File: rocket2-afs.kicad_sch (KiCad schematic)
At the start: 68 parts, among them J1 ARMING_PLUG, J2 POWER, J3 E-MATCH_DROGUE, J4 SWD, J5 E-MATCH_RECOVERY, Q1 Q_NMOS_GSD, Q2 Q_NMOS_GSD, Q3 Q_NMOS_GSD, Q4 Q_NMOS_GSD, Q5 Q_NMOS_GSD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

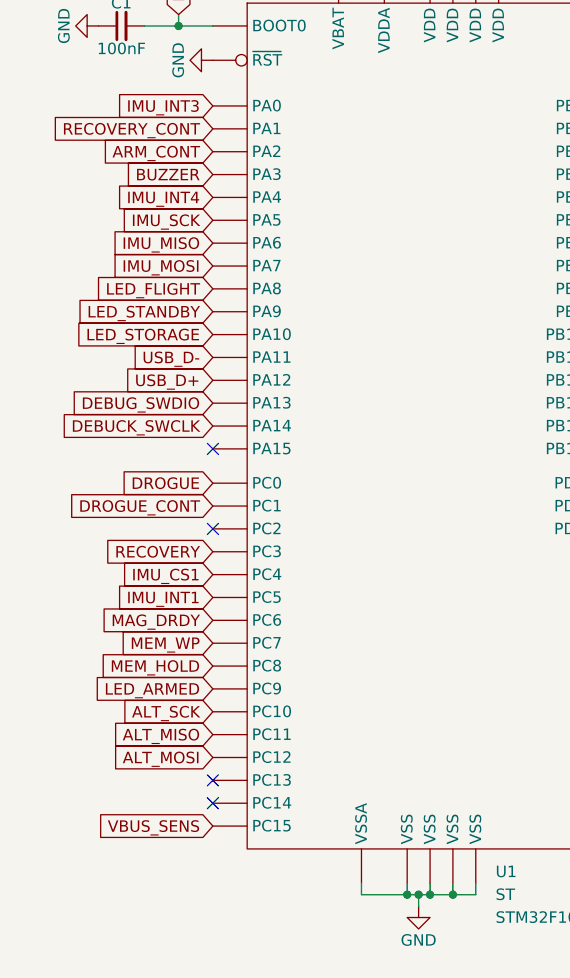
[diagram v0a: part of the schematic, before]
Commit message: Moved All Thick Components to "Front" Layer. Added Silkscreens
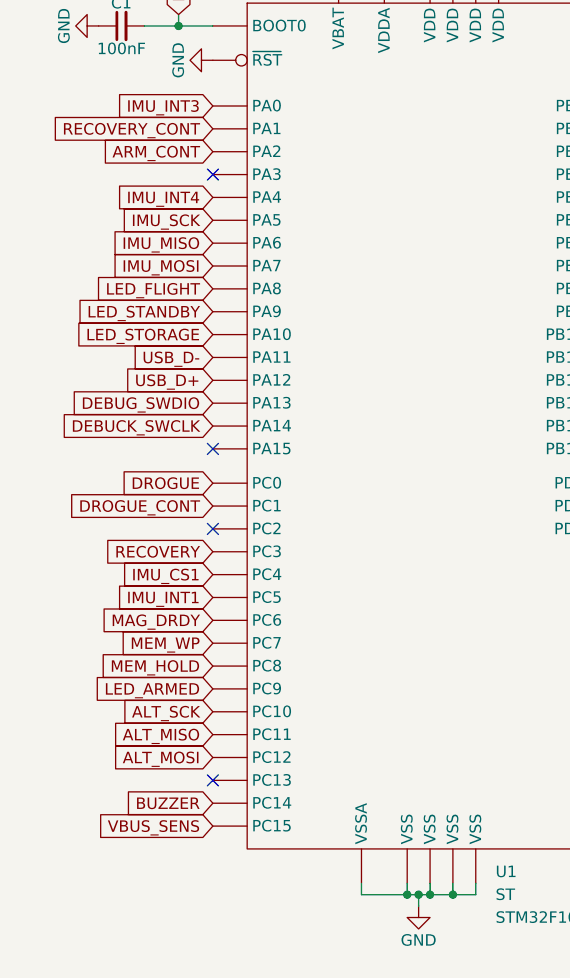
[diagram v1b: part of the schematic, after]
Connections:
- net BUZZER: now also U1.3 (PC14); no longer U1.17 (PA3)
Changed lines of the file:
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@@
   (no_connect (at 173.99 118.11))
   (no_connect (at 78.74 101.6))
+  (no_connect (at 33.02 64.77))
   (no_connect (at 78.74 67.31))
   (no_connect (at 124.46 151.13))
@@
   (no_connect (at 199.39 109.22))
   (no_connect (at 33.02 132.08))
-  (no_connect (at 33.02 134.62))
   (no_connect (at 124.46 153.67))
   (no_connect (at 199.39 111.76))
@@
     )
   )
-  (global_label "BUZZER" (shape input) (at 33.02 64.77 180) (fields_autoplaced)
+  (global_label "BUZZER" (shape input) (at 33.02 134.62 180) (fields_autoplaced)
     (effects (font (size 1.27 1.27)) (justify right))
-    (property "Intersheetrefs" "${INTERSHEET_REFS}" (at 22.5963 64.77 0)
+    (property "Intersheetrefs" "${INTERSHEET_REFS}" (at 22.5963 134.62 0)
       (effects (font (size 1.27 1.27)) (justify right) hide)
     )

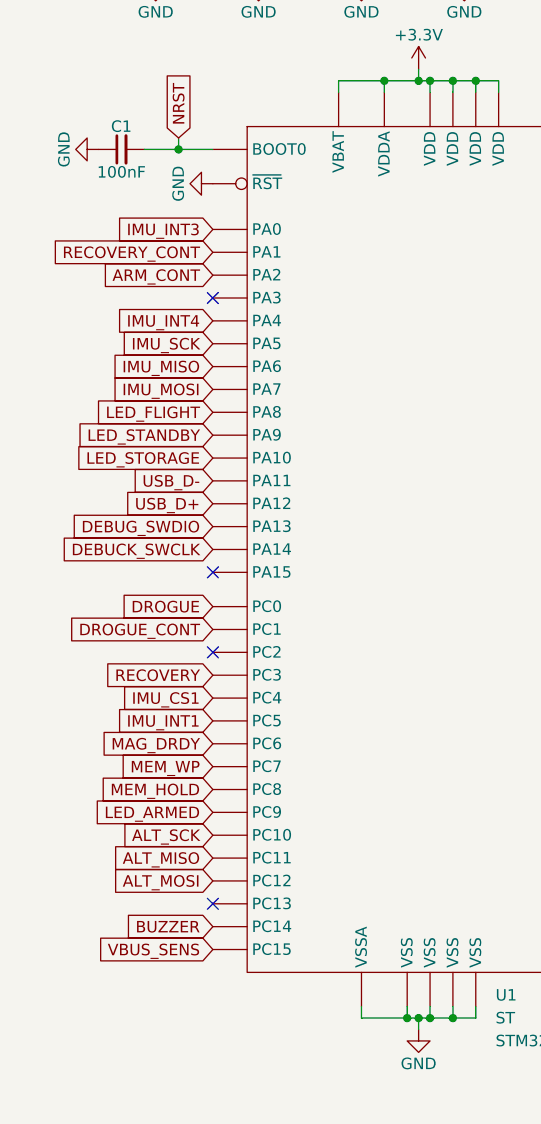
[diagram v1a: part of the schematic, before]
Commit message: Adjusted VBUS
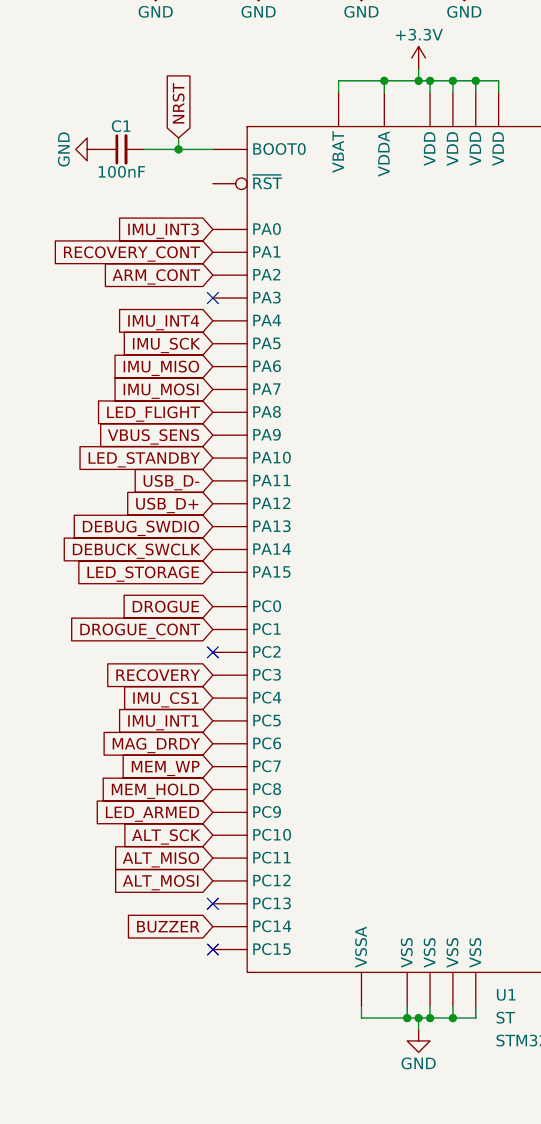
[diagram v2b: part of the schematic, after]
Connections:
- net GND: no longer U1.7 (~{RST})
- net LED_STANDBY: now also U1.43 (PA10); no longer U1.42 (PA9)
- net LED_STORAGE: now also U1.50 (PA15); no longer U1.43 (PA10)
- net VBUS_SENS: now also U1.42 (PA9); no longer U1.4 (PC15)
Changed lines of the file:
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@@
   )
   (no_connect (at 78.74 64.77))
-  (no_connect (at 33.02 95.25))
   (no_connect (at 167.64 53.34))
   (no_connect (at 33.02 104.14))
@@
   (no_connect (at 124.46 151.13))
   (no_connect (at 173.99 115.57))
+  (no_connect (at 33.02 137.16))
   (no_connect (at 199.39 109.22))
   (no_connect (at 33.02 132.08))
@@
     )
   )
-  (global_label "LED_STANDBY" (shape input) (at 33.02 80.01 180) (fields_autoplaced)
-    (effects (font (size 1.27 1.27)) (justify right))
-    (property "Intersheetrefs" "${INTERSHEET_REFS}" (at 17.3953 80.01 0)
+  (global_label "LED_STANDBY" (shape input) (at 33.02 82.55 180) (fields_autoplaced)
+    (effects (font (size 1.27 1.27)) (justify right))
+    (property "Intersheetrefs" "${INTERSHEET_REFS}" (at 17.3953 82.55 0)
       (effects (font (size 1.27 1.27)) (justify right) hide)
     )
@@
     )
   )
-  (global_label "VBUS_SENS" (shape input) (at 33.02 137.16 180) (fields_autoplaced)
-    (effects (font (size 1.27 1.27)) (justify right))
-    (property "Intersheetrefs" "${INTERSHEET_REFS}" (at 19.2701 137.16 0)
+  (global_label "VBUS_SENS" (shape input) (at 33.02 80.01 180) (fields_autoplaced)
+    (effects (font (size 1.27 1.27)) (justify right))
+    (property "Intersheetrefs" "${INTERSHEET_REFS}" (at 19.2701 80.01 0)
       (effects (font (size 1.27 1.27)) (justify right) hide)
     )
@@
     )
   )
-  (global_label "LED_STORAGE" (shape input) (at 33.02 82.55 180) (fields_autoplaced)
-    (effects (font (size 1.27 1.27)) (justify right))
-    (property "Intersheetrefs" "${INTERSHEET_REFS}" (at 17.3349 82.55 0)
+  (global_label "LED_STORAGE" (shape input) (at 33.02 95.25 180) (fields_autoplaced)
+    (effects (font (size 1.27 1.27)) (justify right))
+    (property "Intersheetrefs" "${INTERSHEET_REFS}" (at 17.3349 95.25 0)
       (effects (font (size 1.27 1.27)) (justify right) hide)
     )
@@
         )
       )
-    )
-  )
-  (symbol (lib_id "power:GND") (at 33.02 52.07 270) (unit 1)
-    (in_bom yes) (on_board yes) (dnp no)
-    (property "Reference" "#PWR04" (at 26.67 52.07 0)
-      (effects (font (size 1.27 1.27)) hide)
-    )
-    (property "Value" "GND" (at 29.21 52.07 0)
-      (effects (font (size 1.27 1.27)))
-    )
-    (property "Footprint" "" (at 33.02 52.07 0)
-      (effects (font (size 1.27 1.27)) hide)
-    )
-    (property "Datasheet" "" (at 33.02 52.07 0)
-      (effects (font (size 1.27 1.27)) hide)
-    )
-    (pin "1")
-    (instances
-      (project "rocket2-afs"
-        (path "/bb02b74a-6e6c-4d52-9615-6a7971a5afcd"
-          (reference "#PWR04") (unit 1)
-        )
-      )
-      (project "AFS2.1_Betelgeuse"
-        (path "/be554a08-147d-45c0-b8f6-ea3dd923a785"
-          (reference "#PWR016") (unit 1)
-        )
-      )

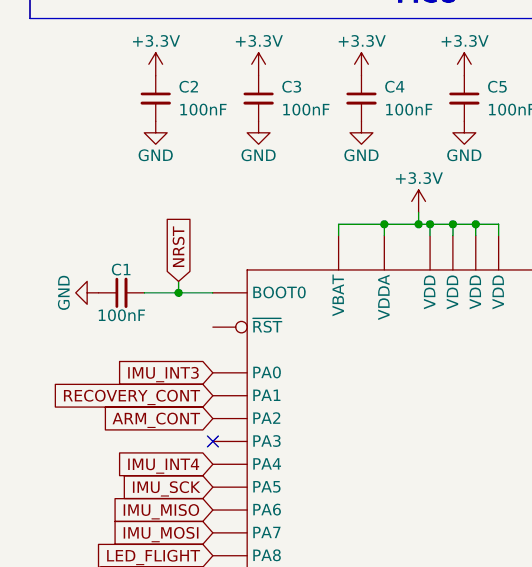
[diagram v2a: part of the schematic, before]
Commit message: Moved BOOT0 Schematic to RST
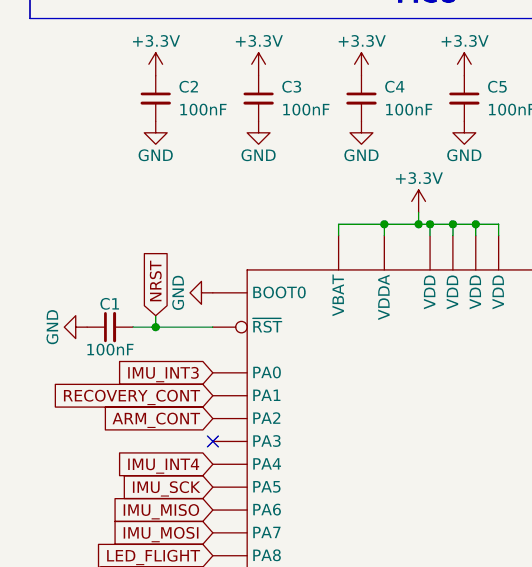
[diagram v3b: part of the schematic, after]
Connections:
- net GND: now also U1.60 (BOOT0)
- net NRST: now also U1.7 (~{RST}); no longer U1.60 (BOOT0)
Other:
- moved on the sheet: C1
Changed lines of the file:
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@@
   (junction (at 238.76 114.3) (diameter 0) (color 0 0 0 0)
   )
-  (junction (at 29.21 48.26) (diameter 0) (color 0 0 0 0)
-  )
   (junction (at 137.16 200.66) (diameter 0) (color 0 0 0 0)
   )
@@
   (junction (at 199.39 92.71) (diameter 0) (color 0 0 0 0)
   )
+  (junction (at 26.67 52.07) (diameter 0) (color 0 0 0 0)
+  )
   (junction (at 57.15 144.78) (diameter 0) (color 0 0 0 0)
   )
@@
     (stroke (width 0) (type default))
   )
-  (wire (pts (xy 29.21 46.99) (xy 29.21 48.26))
-    (stroke (width 0) (type default))
-  )
   (wire (pts (xy 151.13 180.34) (xy 151.13 184.15))
     (stroke (width 0) (type default))
@@
     (stroke (width 0) (type default))
   )
-  (wire (pts (xy 25.4 48.26) (xy 29.21 48.26))
+  (wire (pts (xy 24.13 52.07) (xy 26.67 52.07))
     (stroke (width 0) (type default))
   )
@@
     (stroke (width 0) (type default))
   )
-  (wire (pts (xy 29.21 48.26) (xy 33.02 48.26))
-    (stroke (width 0) (type default))
-  )
   (wire (pts (xy 59.69 143.51) (xy 59.69 144.78))
     (stroke (width 0) (type default))
@@
     (stroke (width 0) (type default))
   )
+  (wire (pts (xy 26.67 50.8) (xy 26.67 52.07))
+    (stroke (width 0) (type default))
+  )
   (wire (pts (xy 49.53 143.51) (xy 49.53 144.78))
     (stroke (width 0) (type default))
@@
     (stroke (width 0) (type default))
   )
+  (wire (pts (xy 26.67 52.07) (xy 33.02 52.07))
+    (stroke (width 0) (type default))
+  )
   (wire (pts (xy 36.83 180.34) (xy 35.56 180.34))
     (stroke (width 0) (type default))
@@
     )
   )
-  (global_label "NRST" (shape input) (at 29.21 46.99 90) (fields_autoplaced)
+  (global_label "NRST" (shape input) (at 26.67 50.8 90) (fields_autoplaced)
     (effects (font (size 1.27 1.27)) (justify left))
-    (property "Intersheetrefs" "${INTERSHEET_REFS}" (at 29.21 39.2272 90)
+    (property "Intersheetrefs" "${INTERSHEET_REFS}" (at 26.67 43.0372 90)
       (effects (font (size 1.27 1.27)) (justify left) hide)
     )
@@
     )
   )
-  (symbol (lib_id "power:GND") (at 20.32 48.26 270) (unit 1)
+  (symbol (lib_id "power:GND") (at 19.05 52.07 270) (unit 1)
     (in_bom yes) (on_board yes) (dnp no)
-    (property "Reference" "#PWR01" (at 13.97 48.26 0)
+    (property "Reference" "#PWR01" (at 12.7 52.07 0)
       (effects (font (size 1.27 1.27)) hide)
     )
-    (property "Value" "GND" (at 16.51 48.26 0)
+    (property "Value" "GND" (at 15.24 52.07 0)
       (effects (font (size 1.27 1.27)))
     )
-    (property "Footprint" "" (at 20.32 48.26 0)
+    (property "Footprint" "" (at 19.05 52.07 0)
       (effects (font (size 1.27 1.27)) hide)
     )
-    (property "Datasheet" "" (at 20.32 48.26 0)
+    (property "Datasheet" "" (at 19.05 52.07 0)
       (effects (font (size 1.27 1.27)) hide)
     )
@@
     )
   )
-  (symbol (lib_id "Device:C_Small") (at 22.86 48.26 90) (unit 1)
+  (symbol (lib_id "Device:C_Small") (at 21.59 52.07 90) (unit 1)
     (in_bom yes) (on_board yes) (dnp no)
-    (property "Reference" "C1" (at 22.86 45.72 90)
+    (property "Reference" "C1" (at 21.59 49.53 90)
       (effects (font (size 1.27 1.27)))
     )
-    (property "Value" "100nF" (at 22.86 50.8 90)
+    (property "Value" "100nF" (at 21.59 54.61 90)
       (effects (font (size 1.27 1.27)))
     )
-    (property "Footprint" "Capacitor_SMD:C_0603_1608Metric" (at 22.86 48.26 0)
+    (property "Footprint" "Capacitor_SMD:C_0603_1608Metric" (at 21.59 52.07 0)
       (effects (font (size 1.27 1.27)) hide)
     )
-    (property "Datasheet" "" (at 22.86 48.26 0)
+    (property "Datasheet" "" (at 21.59 52.07 0)
       (effects (font (size 1.27 1.27)) hide)
     )
-    (property "Manufacturer" "Generic" (at 22.86 48.26 0)
+    (property "Manufacturer" "Generic" (at 21.59 52.07 0)
       (effects (font (size 1.27 1.27)) hide)
     )
-    (property "Part #" "Generic 0603 6.3V 100nF Power Decoupling Cap" (at 22.86 48.26 0)
+    (property "Part #" "Generic 0603 6.3V 100nF Power Decoupling Cap" (at 21.59 52.07 0)
       (effects (font (size 1.27 1.27)) hide)
     )
@@
         )
       )
+    )
+  )
+  (symbol (lib_id "power:GND") (at 33.02 48.26 270) (unit 1)
+    (in_bom yes) (on_board yes) (dnp no)
+    (property "Reference" "#PWR04" (at 26.67 48.26 0)
+      (effects (font (size 1.27 1.27)) hide)
+    )
+    (property "Value" "GND" (at 29.21 48.26 0)
+      (effects (font (size 1.27 1.27)))
+    )
+    (property "Footprint" "" (at 33.02 48.26 0)
+      (effects (font (size 1.27 1.27)) hide)
+    )
+    (property "Datasheet" "" (at 33.02 48.26 0)
+      (effects (font (size 1.27 1.27)) hide)
+    )
+    (pin "1")
+    (instances
+      (project "rocket2-afs"
+        (path "/bb02b74a-6e6c-4d52-9615-6a7971a5afcd"
+          (reference "#PWR04") (unit 1)
+        )
+      )

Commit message: Updated Generic Component Assignment
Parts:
- C10, C9: Part # Generic 0603 6.3V 100nF Power Decoupling Cap -> Generic 0603 6.3V 10uF Power Decoupling Cap
- C21: Part # Generic 0603 6.3V 100nF Power Decoupling Cap -> Generic 0603 6.3V 4.7nF Power Decoupling Cap
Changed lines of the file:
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@@
       (effects (font (size 1.27 1.27)) hide)
     )
-    (property "Part #" "Generic 0603 6.3V 100nF Power Decoupling Cap" (at 134.62 120.65 0)
+    (property "Part #" "Generic 0603 6.3V 10uF Power Decoupling Cap" (at 134.62 120.65 0)
       (effects (font (size 1.27 1.27)) hide)
     )
@@
       (effects (font (size 1.27 1.27)) hide)
     )
-    (property "Part #" "Generic 0603 6.3V 100nF Power Decoupling Cap" (at 111.76 120.65 0)
+    (property "Part #" "Generic 0603 6.3V 10uF Power Decoupling Cap" (at 111.76 120.65 0)
       (effects (font (size 1.27 1.27)) hide)
     )
@@
       (effects (font (size 1.27 1.27)) hide)
     )
-    (property "Part #" "Generic 0603 6.3V 100nF Power Decoupling Cap" (at 157.48 110.49 0)
-      (effects (font (size 1.27 1.27)) hide)
-    )
+    (property "Part #" "Generic 0603 6.3V 4.7nF Power Decoupling Cap" (at 157.48 110.49 0)
+      (effects (font (size 1.27 1.27)) hide)
+    )

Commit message: Updated Generic Component Descriptions
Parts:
- C1, C11, C12, C13, C14, C15, C16, C17, C18, C19, C2, C20, C3, C4, C5, C6, C7, C8: Part # Generic 0603 6.3V 100nF Power Decoupling Cap -> Generic 0603 6.3V 100nF X7R MLCC Capacitor
- C10, C9: Part # Generic 0603 6.3V 10uF Power Decoupling Cap -> Generic 0603 6.3V 10uF X7R MLCC Capacitor
- C21: Part # Generic 0603 6.3V 4.7nF Power Decoupling Cap -> Generic 0603 6.3V 4.7nF X7R MLCC Capacitor
- R1, R12, R3: Part # Generic 0603 1k 5% Res -> Generic 0603 1k 1% Resistor
- R10, R6, R7, R9: Part # Generic 0603 470 5% Res -> Generic 0603 470 1% Resistor
- R11, R19, R4, R5, R8: Part # Generic 0603 10k 5% Res -> Generic 0603 10k 1% Resistor
- R13: Part # Generic 0603 33k 5% Res -> Generic 0603 33k 1% Resistor
- R14: Part # Generic 0603 82k 5% Res -> Generic 0603 82k 1% Resistor
- R15, R16: Part # Generic 0603 5.1k 1% Res -> Generic 0603 5.1k 1% Resistor
- R17, R18: Part # Generic 0603 4.7k 5% Res -> Generic 0603 4.7k 1% Resistor
- R2: Part # Generic 0603 3.3k 5% Res -> Generic 0603 3.3k 1% Resistor
- R20, R21, R22: Part # Generic 0603 100 5% Res -> Generic 0603 100 1% Resistor
